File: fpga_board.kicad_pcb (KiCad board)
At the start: 8 copper layers, 50 x 50 mm, 10 parts, among them U1 LFE5U-45F-7BG256I, U10 TLV62569DRL, U2 CYUSB3014-BZXC, U3 K4B4G1646E-BCMA, U4 K4B4G1646E-BCMA, U5 K4B4G1646E-BCMA, U6 K4B4G1646E-BCMA, U7 TLV62569DRL, U8 TLV62569DRL, U9 TLV62569DRL

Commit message: added spi pins and FX3 crystal capacitors and allat and idk other stuff
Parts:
- removed U3, U4: K4B4G1646E-BCMA, Package_BGA:Micron_FBGA-96_7.5x13.5mm_Layout9x16_P0.8mm
- added D2: LED_RGBA, LED_SMD:LED_Wurth_150044M155260, F.Cu at (59.6, 34.4)
- added J1: USB3_A, Connector_USB:USB3_A_Molex_48393-001, F.Cu at (107.0, 27.3)
- added X1: XO32, Crystal:Crystal_SMD_5032-4Pin_5.0x3.2mm, F.Cu at (61.5, 30.6)
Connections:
- U1 pad D8: unconnected-(U1C-PT42B-PadD8) -> GPIO_23
- U1 pad L6: unconnected-(U1D-VCCIO8-PadL6) -> 3v3
- U1 pad M10: unconnected-(U1C-TDO-PadM10) -> JTAG.TDO
- U1 pad N9: unconnected-(U1A-CCLK-PadN9) -> SPI.SCK
- U1 pad P9: unconnected-(U1A-DONE-PadP9) -> Net-(U1A-DONE)
- U1 pad R11: unconnected-(U1A-TDI-PadR11) -> JTAG.TDI
- U1 pad R8: unconnected-(U1A-PB13A-PadR8) -> Net-(U1A-PB13A)
- U1 pad R9: unconnected-(U1A-PROGRAMN-PadR9) -> Net-(U1A-PROGRAMN)
- U1 pad T10: unconnected-(U1A-TCK-PadT10) -> JTAG.TCK
- U1 pad T11: unconnected-(U1A-TMS-PadT11) -> JTAG.TMS
- U1 pad T6: unconnected-(U1A-PB4A-PadT6) -> FPGA_CLK
- U1 pad T7: unconnected-(U1A-PB11A-PadT7) -> SPI.MISO
- U1 pad T8: unconnected-(U1A-PB11B-PadT8) -> SPI.MOSI
- U1 pad T9: unconnected-(U1A-INITN-PadT9) -> Net-(U1A-INITN)
- U2 pad A10: unconnected-(U2A-DM-PadA10) -> D_N
- U2 pad A9: unconnected-(U2A-DP-PadA9) -> D_P
- U2 pad B1: unconnected-(U2B-VIO4-PadB1) -> 3v3
- U2 pad C5: unconnected-(U2A-RESET#-PadC5) -> RESET#
- U2 pad E3: unconnected-(U2B-VIO3-PadE3) -> 3v3
- U2 pad F1: FX3_VIO1-2_3v3 -> 3v3
- U2 pad G5: unconnected-(U2B-GPIO[25]-PadG5) -> GPIO25
- U2 pad H11: FX3_VIO1-2_3v3 -> 3v3
- U2 pad H6: unconnected-(U2B-GPIO[26]-PadH6) -> GPIO26
- U2 pad K5: unconnected-(U2B-GPIO[27]-PadK5) -> GPIO27
- U2 pad K6: unconnected-(U2B-GPIO[23]-PadK6) -> GPIO_23
- U2 pad L9: FX3_VIO1-2_3v3 -> 3v3
- U5 pad A1: unconnected-(U5B-VDDQ-PadA1) -> 1v35
- U5 pad A8: unconnected-(U5B-VDDQ-PadA8) -> 1v35
- U5 pad A9: unconnected-(U5C-VSS-PadA9) -> GND
- U5 pad B1: unconnected-(U5C-VSSQ-PadB1) -> GND
- U5 pad B2: unconnected-(U5B-VDD-PadB2) -> 1v35
- U5 pad B3: unconnected-(U5C-VSS-PadB3) -> GND
- U5 pad B9: unconnected-(U5C-VSSQ-PadB9) -> GND
- U5 pad C1: unconnected-(U5B-VDDQ-PadC1) -> 1v35
- U5 pad C9: unconnected-(U5B-VDDQ-PadC9) -> 1v35
- U5 pad D1: unconnected-(U5C-VSSQ-PadD1) -> GND
- U5 pad D2: unconnected-(U5B-VDDQ-PadD2) -> 1v35
- U5 pad D8: unconnected-(U5C-VSSQ-PadD8) -> GND
- U5 pad D9: unconnected-(U5B-VDD-PadD9) -> 1v35
- U5 pad E1: unconnected-(U5C-VSS-PadE1) -> GND
- U5 pad E2: unconnected-(U5C-VSSQ-PadE2) -> GND
- U5 pad E8: unconnected-(U5C-VSSQ-PadE8) -> GND
- U5 pad E9: unconnected-(U5B-VDDQ-PadE9) -> 1v35
- U5 pad F1: unconnected-(U5B-VDDQ-PadF1) -> 1v35
- U5 pad F9: unconnected-(U5C-VSSQ-PadF9) -> GND
- U5 pad G1: unconnected-(U5C-VSSQ-PadG1) -> GND
- U5 pad G7: unconnected-(U5B-VDD-PadG7) -> 1v35
- U5 pad G8: unconnected-(U5C-VSS-PadG8) -> GND
- U5 pad G9: unconnected-(U5C-VSSQ-PadG9) -> GND
- U5 pad H1: unconnected-(U5B-VREFDQ-PadH1) -> DRAM_VREF
- U5 pad H2: unconnected-(U5B-VDDQ-PadH2) -> 1v35
- U5 pad H9: unconnected-(U5B-VDDQ-PadH9) -> 1v35
- U5 pad J2: unconnected-(U5C-VSS-PadJ2) -> GND
- U5 pad J3: unconnected-(U5A-*RAS-PadJ3) -> #RAS
- U5 pad J7: unconnected-(U5A-CK-PadJ7) -> CK
- U5 pad J8: unconnected-(U5C-VSS-PadJ8) -> GND
- U5 pad K2: unconnected-(U5B-VDD-PadK2) -> 1v35
- U5 pad K3: unconnected-(U5A-*CAS-PadK3) -> #CAS
- U5 pad K7: unconnected-(U5A-*CK-PadK7) -> #CK
- U5 pad K8: unconnected-(U5B-VDD-PadK8) -> 1v35
- U5 pad K9: unconnected-(U5A-CKE-PadK9) -> CKE
- U5 pad L2: unconnected-(U5A-*CS-PadL2) -> #CS
- U5 pad L3: unconnected-(U5A-*WE-PadL3) -> #WE
- U5 pad L7: unconnected-(U5A-A10/AP-PadL7) -> A10
- U5 pad L8: unconnected-(U5B-ZQ-PadL8) -> Net-(U5B-ZQ)
- U5 pad M1: unconnected-(U5C-VSS-PadM1) -> GND
- U5 pad M2: unconnected-(U5A-BA0-PadM2) -> BA0
- U5 pad M3: unconnected-(U5A-BA2-PadM3) -> BA2
- U5 pad M8: unconnected-(U5B-VREFCA-PadM8) -> DRAM_VREF
- U5 pad M9: unconnected-(U5C-VSS-PadM9) -> GND
- U5 pad N1: unconnected-(U5B-VDD-PadN1) -> 1v35
- U5 pad N2: unconnected-(U5A-A3-PadN2) -> A3
- U5 pad N3: unconnected-(U5A-A0-PadN3) -> A0
- U5 pad N7: unconnected-(U5A-A12/*BC-PadN7) -> A12
- U5 pad N8: unconnected-(U5A-BA1-PadN8) -> BA1
- U5 pad N9: unconnected-(U5B-VDD-PadN9) -> 1v35
- U5 pad P1: unconnected-(U5C-VSS-PadP1) -> GND
- U5 pad P2: unconnected-(U5A-A5-PadP2) -> A5
- U5 pad P3: unconnected-(U5A-A2-PadP3) -> A2
- U5 pad P7: unconnected-(U5A-A1-PadP7) -> A1
- U5 pad P8: unconnected-(U5A-A4-PadP8) -> A4
- U5 pad P9: unconnected-(U5C-VSS-PadP9) -> GND
- U5 pad R1: unconnected-(U5B-VDD-PadR1) -> 1v35
- U5 pad R2: unconnected-(U5A-A7-PadR2) -> A7
- U5 pad R3: unconnected-(U5A-A9-PadR3) -> A9
- U5 pad R7: unconnected-(U5A-A11-PadR7) -> A11
- U5 pad R8: unconnected-(U5A-A6-PadR8) -> A6
- U5 pad R9: unconnected-(U5B-VDD-PadR9) -> 1v35
- U5 pad T1: unconnected-(U5C-VSS-PadT1) -> GND
- U5 pad T2: unconnected-(U5A-*RESET-PadT2) -> #RESET
- U5 pad T3: unconnected-(U5A-A13-PadT3) -> A13
- U5 pad T7: unconnected-(U5A-A14-PadT7) -> A14
- U5 pad T8: unconnected-(U5A-A8-PadT8) -> A8
- U5 pad T9: unconnected-(U5C-VSS-PadT9) -> GND
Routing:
- net unconnected-(U1C-PT42B-PadD8): track 0.57 -> 0.00 mm, vias 1 -> 0
- net GPIO_23: track 0.00 -> 0.57 mm, vias 0 -> 1

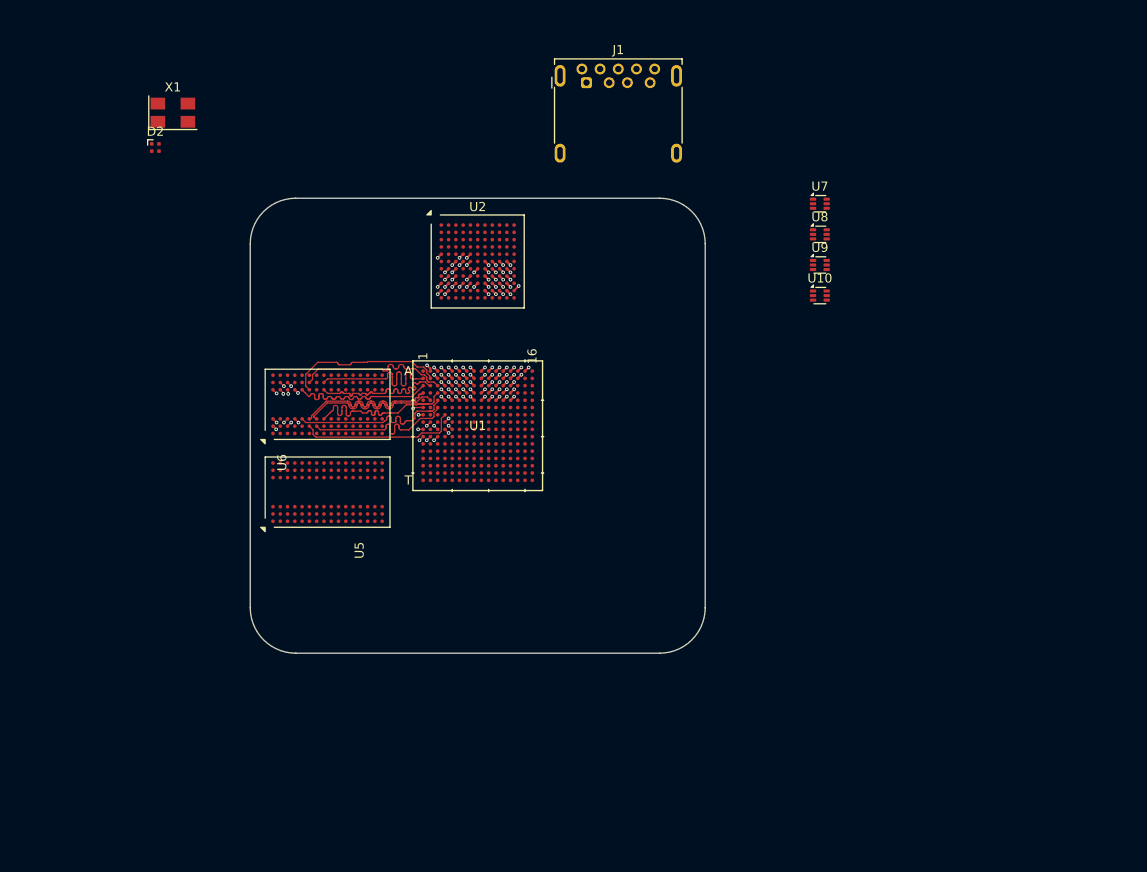
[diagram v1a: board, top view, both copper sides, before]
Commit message: added capacitor and resistor footprints
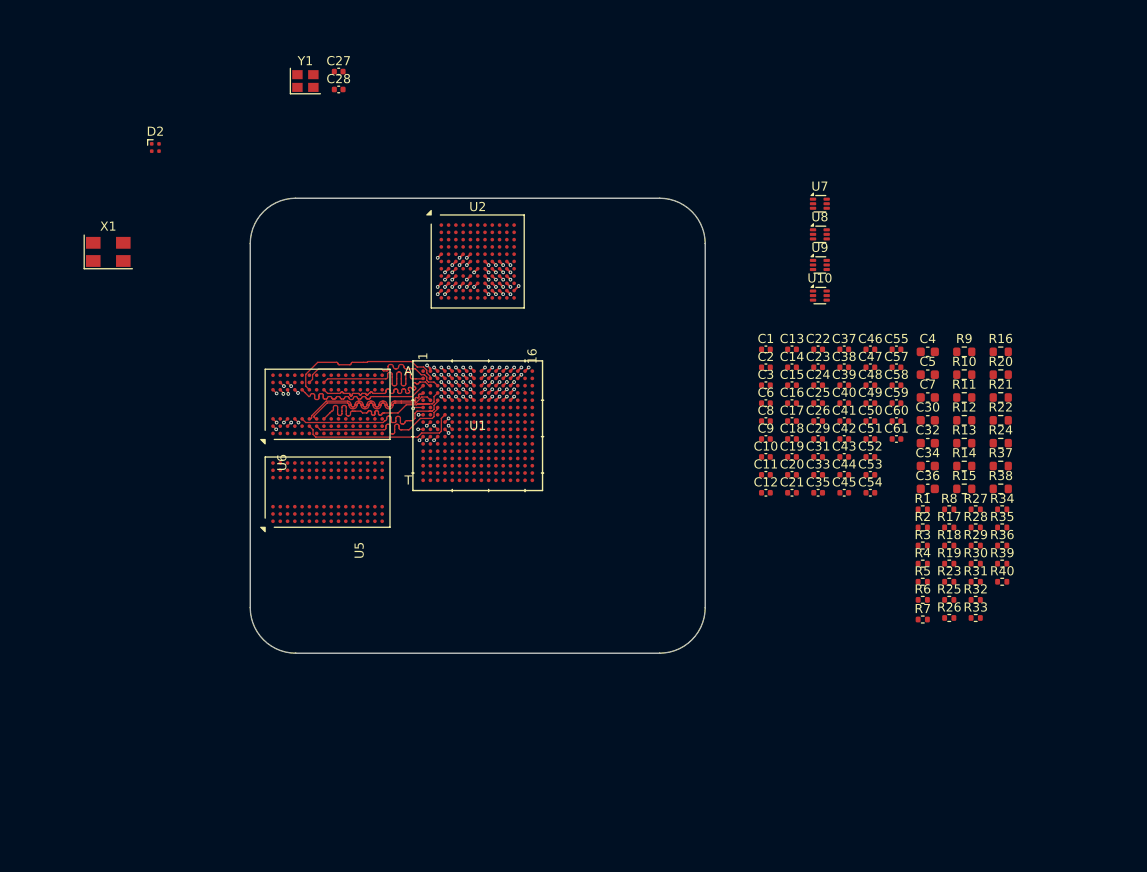
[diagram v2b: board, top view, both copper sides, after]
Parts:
- removed J1: USB3_A, Connector_USB:USB3_A_Molex_48393-001
- added C1: 0.1µF, Capacitor_SMD:C_0402_1005Metric, F.Cu at (126.7, 56.6)
- added C10: 0.1µF, Capacitor_SMD:C_0402_1005Metric, F.Cu at (126.7, 68.4)
- added C11: 0.01µF, Capacitor_SMD:C_0402_1005Metric, F.Cu at (126.7, 70.4)
- added C12: 0.1µF, Capacitor_SMD:C_0402_1005Metric, F.Cu at (126.7, 72.4)
- added C13: 0.1µF, Capacitor_SMD:C_0402_1005Metric, F.Cu at (129.5, 56.6)
- added C14: 0.1µF, Capacitor_SMD:C_0402_1005Metric, F.Cu at (129.5, 58.6)
- added C15: 2.2µF, Capacitor_SMD:C_0402_1005Metric, F.Cu at (129.5, 60.5)
- added C16: 0.1µF, Capacitor_SMD:C_0402_1005Metric, F.Cu at (129.5, 62.5)
- added C17: 0.1µF, Capacitor_SMD:C_0402_1005Metric, F.Cu at (129.5, 64.5)
- added C18: 0.01µF, Capacitor_SMD:C_0402_1005Metric, F.Cu at (129.5, 66.5)
- added C19: 0.01µF, Capacitor_SMD:C_0402_1005Metric, F.Cu at (129.5, 68.4)
- added C2: 0.1µF, Capacitor_SMD:C_0402_1005Metric, F.Cu at (126.7, 58.6)
- added C20: 0.1µF, Capacitor_SMD:C_0402_1005Metric, F.Cu at (129.5, 70.4)
- added C21: 0.1µF, Capacitor_SMD:C_0402_1005Metric, F.Cu at (129.5, 72.4)
- added C22: 0.01µF, Capacitor_SMD:C_0402_1005Metric, F.Cu at (132.4, 56.6)
- added C23: 0.1µF, Capacitor_SMD:C_0402_1005Metric, F.Cu at (132.4, 58.6)
- added C24: 0.1µF, Capacitor_SMD:C_0402_1005Metric, F.Cu at (132.4, 60.5)
- added C25: 0.1µF, Capacitor_SMD:C_0402_1005Metric, F.Cu at (132.4, 62.5)
- added C26: 0.01µF, Capacitor_SMD:C_0402_1005Metric, F.Cu at (132.4, 64.5)
- added C27: 15pF, Capacitor_SMD:C_0402_1005Metric, F.Cu at (79.7, 26.1)
- added C28: 15pF, Capacitor_SMD:C_0402_1005Metric, F.Cu at (79.7, 28.1)
- added C29: 4.7µF, Capacitor_SMD:C_0402_1005Metric, F.Cu at (132.4, 66.5)
- added C3: 0.1µF, Capacitor_SMD:C_0402_1005Metric, F.Cu at (126.7, 60.5)
- added C30: 10µF, Capacitor_SMD:C_0603_1608Metric, F.Cu at (144.5, 64.4)
- added C31: 4.7µF, Capacitor_SMD:C_0402_1005Metric, F.Cu at (132.4, 68.4)
- added C32: 10µF, Capacitor_SMD:C_0603_1608Metric, F.Cu at (144.5, 66.9)
- added C33: 4.7µF, Capacitor_SMD:C_0402_1005Metric, F.Cu at (132.4, 70.4)
- added C34: 10µF, Capacitor_SMD:C_0603_1608Metric, F.Cu at (144.5, 69.4)
- added C35: 4.7µF, Capacitor_SMD:C_0402_1005Metric, F.Cu at (132.4, 72.4)
- added C36: 10µF, Capacitor_SMD:C_0603_1608Metric, F.Cu at (144.5, 71.9)
- added C37: 4.7µF, Capacitor_SMD:C_0402_1005Metric, F.Cu at (135.3, 56.6)
- added C38: 0.1µF, Capacitor_SMD:C_0402_1005Metric, F.Cu at (135.3, 58.6)
- added C39: 0.1µF, Capacitor_SMD:C_0402_1005Metric, F.Cu at (135.3, 60.5)
- added C4: 22µF, Capacitor_SMD:C_0603_1608Metric, F.Cu at (144.5, 56.9)
- added C40: 0.1µF, Capacitor_SMD:C_0402_1005Metric, F.Cu at (135.3, 62.5)
- added C41: 0.1µF, Capacitor_SMD:C_0402_1005Metric, F.Cu at (135.3, 64.5)
- added C42: 4.7µF, Capacitor_SMD:C_0402_1005Metric, F.Cu at (135.3, 66.5)
- added C43: 4.7µF, Capacitor_SMD:C_0402_1005Metric, F.Cu at (135.3, 68.4)
- added C44: 0.1µF, Capacitor_SMD:C_0402_1005Metric, F.Cu at (135.3, 70.4)
- added C45: 0.1µF, Capacitor_SMD:C_0402_1005Metric, F.Cu at (135.3, 72.4)
- added C46: 0.1µF, Capacitor_SMD:C_0402_1005Metric, F.Cu at (138.2, 56.6)
- added C47: 0.1µF, Capacitor_SMD:C_0402_1005Metric, F.Cu at (138.2, 58.6)
- added C48: 0.1µF, Capacitor_SMD:C_0402_1005Metric, F.Cu at (138.2, 60.5)
- added C49: 0.1µF, Capacitor_SMD:C_0402_1005Metric, F.Cu at (138.2, 62.5)
- added C5: 22µF, Capacitor_SMD:C_0603_1608Metric, F.Cu at (144.5, 59.4)
- added C50: 0.1µF, Capacitor_SMD:C_0402_1005Metric, F.Cu at (138.2, 64.5)
- added C51: 0.1µF, Capacitor_SMD:C_0402_1005Metric, F.Cu at (138.2, 66.5)
- added C52: 0.1µF, Capacitor_SMD:C_0402_1005Metric, F.Cu at (138.2, 68.4)
- added C53: 4.7µF, Capacitor_SMD:C_0402_1005Metric, F.Cu at (138.2, 70.4)
- added C54: 4.7µF, Capacitor_SMD:C_0402_1005Metric, F.Cu at (138.2, 72.4)
- added C55: 4.7µF, Capacitor_SMD:C_0402_1005Metric, F.Cu at (141.0, 56.6)
- added C57: 0.1µF, Capacitor_SMD:C_0402_1005Metric, F.Cu at (141.0, 58.6)
- added C58: 10pF, Capacitor_SMD:C_0402_1005Metric, F.Cu at (141.0, 60.5)
- added C59: 0.1µF, Capacitor_SMD:C_0402_1005Metric, F.Cu at (141.0, 62.5)
- added C6: 0.1µF, Capacitor_SMD:C_0402_1005Metric, F.Cu at (126.7, 62.5)
- added C60: 0.1µF, Capacitor_SMD:C_0402_1005Metric, F.Cu at (141.0, 64.5)
- added C61: 2.2nF, Capacitor_SMD:C_0402_1005Metric, F.Cu at (141.0, 66.5)
- added C7: 22µF, Capacitor_SMD:C_0603_1608Metric, F.Cu at (144.5, 61.9)
- added C8: 0.01µF, Capacitor_SMD:C_0402_1005Metric, F.Cu at (126.7, 64.5)
- added C9: 0.01µF, Capacitor_SMD:C_0402_1005Metric, F.Cu at (126.7, 66.5)
- added R1: 6k04, Resistor_SMD:R_0402_1005Metric, F.Cu at (143.9, 74.2)
- added R10: 100k, Resistor_SMD:R_0603_1608Metric, F.Cu at (148.5, 59.4)
- added R11: 442k, Resistor_SMD:R_0603_1608Metric, F.Cu at (148.5, 61.9)
- added R12: 100k, Resistor_SMD:R_0603_1608Metric, F.Cu at (148.5, 64.4)
- added R13: 124k, Resistor_SMD:R_0603_1608Metric, F.Cu at (148.5, 66.9)
- added R14: 100k, Resistor_SMD:R_0603_1608Metric, F.Cu at (148.5, 69.4)
- added R15: 82k5, Resistor_SMD:R_0603_1608Metric, F.Cu at (148.5, 71.9)
- added R16: 100k, Resistor_SMD:R_0603_1608Metric, F.Cu at (152.5, 56.9)
- added R17: 4k7, Resistor_SMD:R_0402_1005Metric, F.Cu at (146.8, 76.2)
- added R18: 0, Resistor_SMD:R_0402_1005Metric, F.Cu at (146.8, 78.2)
- added R19: 0, Resistor_SMD:R_0402_1005Metric, F.Cu at (146.8, 80.2)
- added R2: 200, Resistor_SMD:R_0402_1005Metric, F.Cu at (143.9, 76.2)
- added R20: 1k, Resistor_SMD:R_0603_1608Metric, F.Cu at (152.5, 59.4)
- added R21: 1k, Resistor_SMD:R_0603_1608Metric, F.Cu at (152.5, 61.9)
- added R22: 240, Resistor_SMD:R_0603_1608Metric, F.Cu at (152.5, 64.4)
- added R23: 4k7, Resistor_SMD:R_0402_1005Metric, F.Cu at (146.8, 82.2)
- added R24: 1k, Resistor_SMD:R_0603_1608Metric, F.Cu at (152.5, 66.9)
- added R25: 4k7, Resistor_SMD:R_0402_1005Metric, F.Cu at (146.8, 84.1)
- added R26: 0, Resistor_SMD:R_0402_1005Metric, F.Cu at (146.8, 86.1)
- added R27: 0, Resistor_SMD:R_0402_1005Metric, F.Cu at (149.7, 74.2)
- added R28: 4k7, Resistor_SMD:R_0402_1005Metric, F.Cu at (149.7, 76.2)
- added R29: 4k7, Resistor_SMD:R_0402_1005Metric, F.Cu at (149.7, 78.2)
- added R3: 0, Resistor_SMD:R_0402_1005Metric, F.Cu at (143.9, 78.2)
- added R30: 10k, Resistor_SMD:R_0402_1005Metric, F.Cu at (149.7, 80.2)
- added R31: 10k, Resistor_SMD:R_0402_1005Metric, F.Cu at (149.7, 82.2)
- added R32: 20, Resistor_SMD:R_0402_1005Metric, F.Cu at (149.7, 84.1)
- added R33: 10k, Resistor_SMD:R_0402_1005Metric, F.Cu at (149.7, 86.1)
- added R34: 20, Resistor_SMD:R_0402_1005Metric, F.Cu at (152.6, 74.2)
- added R35: 10k, Resistor_SMD:R_0402_1005Metric, F.Cu at (152.6, 76.2)
- added R36: 62, Resistor_SMD:R_0402_1005Metric, F.Cu at (152.6, 78.2)
- added R37: 240, Resistor_SMD:R_0603_1608Metric, F.Cu at (152.5, 69.4)
- added R38: 100k, Resistor_SMD:R_0603_1608Metric, F.Cu at (152.5, 71.9)
- added R39: 5k1, Resistor_SMD:R_0402_1005Metric, F.Cu at (152.6, 80.2)
- added R4: 0, Resistor_SMD:R_0402_1005Metric, F.Cu at (143.9, 80.2)
- added R40: 330, Resistor_SMD:R_0402_1005Metric, F.Cu at (152.6, 82.2)
- added R5: 0, Resistor_SMD:R_0402_1005Metric, F.Cu at (143.9, 82.2)
- added R6: 0, Resistor_SMD:R_0402_1005Metric, F.Cu at (143.9, 84.1)
- added R7: 0, Resistor_SMD:R_0402_1005Metric, F.Cu at (143.9, 86.3)
- added R8: 0, Resistor_SMD:R_0402_1005Metric, F.Cu at (146.8, 74.2)
- added R9: 100k, Resistor_SMD:R_0603_1608Metric, F.Cu at (148.5, 56.9)
- added Y1: Crystal_GND24, Crystal:Crystal_SMD_2520-4Pin_2.5x2.0mm, F.Cu at (76.1, 27.1)
- moved X1 16.9 mm to (54.4, 45.9)
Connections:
- U1 pad P9: Net-(U1A-DONE) -> DONE
- U1 pad T9: Net-(U1A-INITN) -> INIT
- U2 pad D1: unconnected-(U2B-GPIO[50]-PadD1) -> DONE
- U2 pad D2: unconnected-(U2B-GPIO[51]-PadD2) -> PROGRAMN
- U2 pad D3: unconnected-(U2B-GPIO[52]-PadD3) -> INIT

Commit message: added RGB LED for FPGA, added termintaion to FPGA crystal
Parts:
- removed C58: 10pF, Capacitor_SMD:C_0402_1005Metric
- added D1: LED_RGBA, LED_SMD:LED_Wurth_150044M155260, F.Cu at (116.5, 23.0)
- added L1: BLM18KG601SN1D, Inductor_SMD:L_0603_1608Metric, F.Cu at (164.7, 27.1)
- added L2: BLM18KG601SN1D, Inductor_SMD:L_0603_1608Metric, F.Cu at (164.7, 29.6)
- added L3: BLM18KG601SN1D, Inductor_SMD:L_0603_1608Metric, F.Cu at (164.7, 32.1)
- added L4: BLM18KG601SN1D, Inductor_SMD:L_0603_1608Metric, F.Cu at (164.7, 34.6)
- added L5: 2.2µH, Inductor:IND_VLS3015_TDK, F.Cu at (160.3, 28.2)
- added L6: 2.2µH, Inductor:IND_VLS3015_TDK, F.Cu at (160.3, 33.0)
- added L7: 2.2µH, Inductor:IND_VLS3015_TDK, F.Cu at (160.3, 37.7)
- added L8: 2.2µH, Inductor:IND_VLS3015_TDK, F.Cu at (160.3, 42.5)
- added R41: 10k, Resistor_SMD:R_0402_1005Metric, F.Cu at (113.6, 22.6)
- added R42: 10k, Resistor_SMD:R_0402_1005Metric, F.Cu at (113.6, 24.6)
- added R43: 10k, Resistor_SMD:R_0402_1005Metric, F.Cu at (113.6, 26.6)
- added R44: 62, Resistor_SMD:R_0402_1005Metric, F.Cu at (113.6, 28.6)
- added R45: 20, Resistor_SMD:R_0402_1005Metric, F.Cu at (113.6, 30.6)
- added R46: 20, Resistor_SMD:R_0402_1005Metric, F.Cu at (113.6, 32.5)
- added R47: 20, Resistor_SMD:R_0402_1005Metric, F.Cu at (164.8, 50.1)
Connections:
- R17 pad 1: VCCIO8 -> 3v3
- R23 pad 2: VCCIO8 -> 3v3
- R25 pad 2: VCCIO8 -> 3v3
- R28 pad 2: VCCIO8 -> 3v3
- R40 pad 2: VCCIO8 -> 3v3
- U1 pad D10: unconnected-(U1C-PT56A-PadD10) -> FPGA.R
- U1 pad D11: unconnected-(U1C-PT69A-PadD11) -> FPGA.B
- U1 pad E10: unconnected-(U1C-PT56B-PadE10) -> FPGA.G
- X1 pad 3: FPGA_CLK -> Net-(X1-OUT)
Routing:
- net unconnected-(U1C-PT69A-PadD11): track 0.57 -> 0.00 mm, vias 1 -> 0
- net FPGA.B: track 0.00 -> 0.57 mm, vias 0 -> 1
- net unconnected-(U1C-PT56B-PadE10): track 0.57 -> 0.00 mm, vias 1 -> 0
- net unconnected-(U1C-PT56A-PadD10): track 0.57 -> 0.00 mm, vias 1 -> 0
- net FPGA.R: track 0.00 -> 0.57 mm, vias 0 -> 1
- net FPGA.G: track 0.00 -> 0.57 mm, vias 0 -> 1

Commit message: finished schematic, finished BOM.
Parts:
- added C56: 0.1µF, Capacitor_SMD:C_0402_1005Metric, F.Cu at (131.0, 97.6)
- added H1: PH2.54-2X3P-H25, PIN-HEADER:HDR-TH_6P-P2.54-V-M-R2-C3-S2.54-1, F.Cu at (78.0, 84.4)
- added Q1: 2N7002PW, Package_TO_SOT_SMD:SOT-323_SC-70, F.Cu at (127.3, 91.5)
- added Q2: 2N7002PW, Package_TO_SOT_SMD:SOT-323_SC-70, F.Cu at (127.3, 95.4)
- added Q3: 2N7002PW, Package_TO_SOT_SMD:SOT-323_SC-70, F.Cu at (127.3, 99.2)
- added Q4: 2N7002PW, Package_TO_SOT_SMD:SOT-323_SC-70, F.Cu at (127.3, 103.1)
- added Q5: 2N7002PW, Package_TO_SOT_SMD:SOT-323_SC-70, F.Cu at (127.3, 106.9)
- added Q6: 2N7002PW, Package_TO_SOT_SMD:SOT-323_SC-70, F.Cu at (127.3, 110.8)
- added SW1: 1TS028A-1300-0600-CT, BUTTON:SW-SMD_4P-L2.8-W1.9-P1.20-LS3.0_1TS028A, F.Cu at (92.8, 95.5)
- added TP1: TestPoint, TestPoint:TestPoint_Pad_D1.0mm, F.Cu at (131.3, 91.2)
- added TP2: TestPoint, TestPoint:TestPoint_Pad_D1.0mm, F.Cu at (131.3, 94.8)
- added TP3: TestPoint, TestPoint:TestPoint_Pad_D1.0mm, F.Cu at (134.8, 91.2)
- added TP4: TestPoint, TestPoint:TestPoint_Pad_D1.0mm, F.Cu at (134.8, 94.8)
- added TP5: TestPoint, TestPoint:TestPoint_Pad_D1.0mm, F.Cu at (138.4, 91.2)
- added TP6: TestPoint, TestPoint:TestPoint_Pad_D1.0mm, F.Cu at (138.4, 94.8)
- added USB1: TYPE-C 24P QT 143, USB-TYPE-C:TYPE-C-SMD_C9900025773, F.Cu at (102.2, 34.9)
- moved X1 1.33 mm to (55.6, 45.5)
